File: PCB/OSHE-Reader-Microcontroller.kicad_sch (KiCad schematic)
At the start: 5 parts

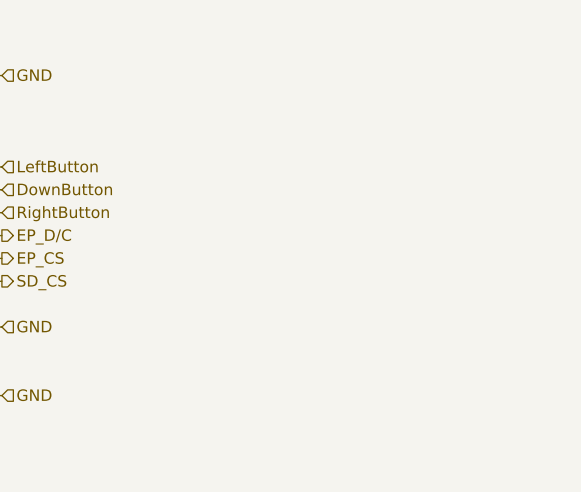
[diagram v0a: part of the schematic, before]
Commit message: Added a bunch of test points to schematic and pcb, hopefully not needed, but good to have :)
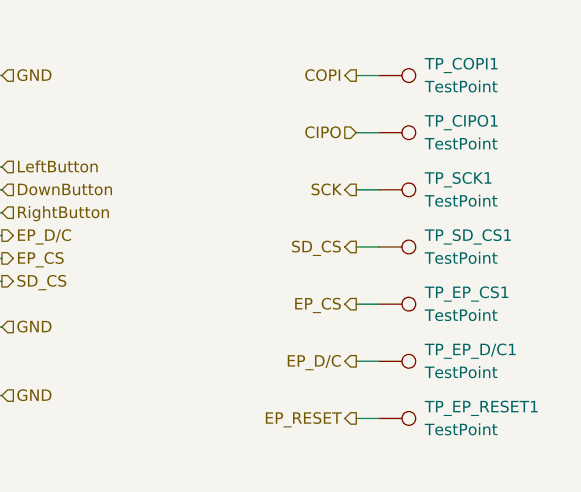
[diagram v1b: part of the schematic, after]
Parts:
- added TP_CIPO1, TP_COPI1, TP_EP_CS1, TP_EP_D/C1, TP_EP_RESET1, TP_SCK1, TP_SD_CS1: TestPoint, TestPoint:TestPoint_Keystone_5019_Miniature, symbol Connector:TestPoint
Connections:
- net CIPO: now also TP_CIPO1.1
- net COPI: now also TP_COPI1.1
- net EP_CS: now also TP_EP_CS1.1
- net EP_D/C: now also TP_EP_D/C1.1
- net EP_RESET: now also TP_EP_RESET1.1
- net SCK: now also TP_SCK1.1
- net SD_CS: now also TP_SD_CS1.1

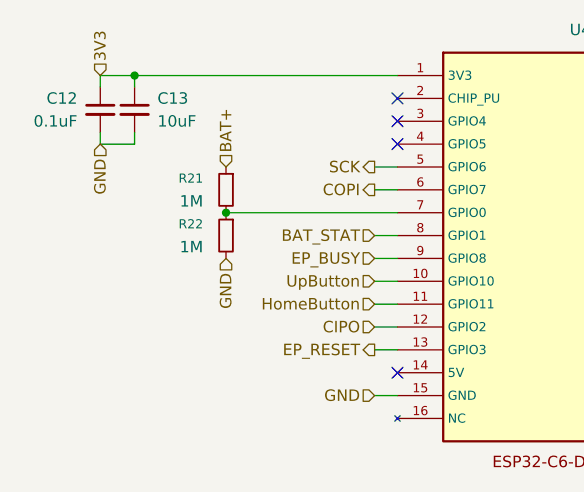
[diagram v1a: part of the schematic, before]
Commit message: Finishing touches with renaming some components and making auto BOM look cleaner
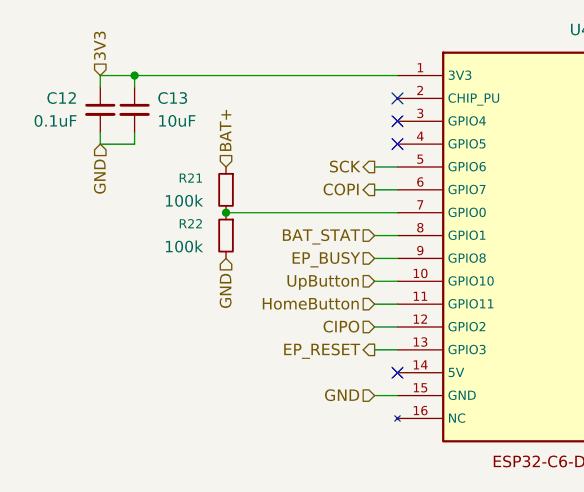
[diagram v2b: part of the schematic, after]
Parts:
- R21, R22: value 1M -> 100k
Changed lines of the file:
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@@
 			)
 		)
-		(property "Value" "1M"
+		(property "Value" "100k"
 			(at 41.91 68.5799 0)
 			(effects
@@
 			)
 		)
-		(property "Value" "1M"
+		(property "Value" "100k"
 			(at 41.91 63.4999 0)
 			(effects

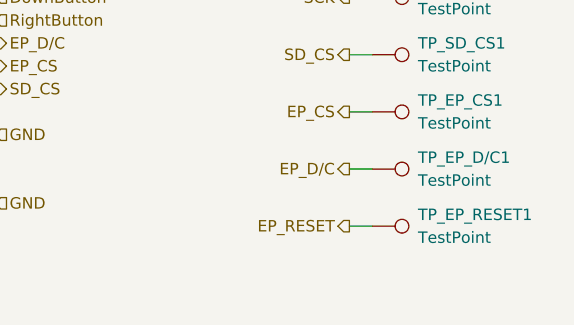
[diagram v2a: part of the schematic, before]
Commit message: Shuffled display connector around for fitting EPD ribbon cable position (also imported dxf for screen + bracket)
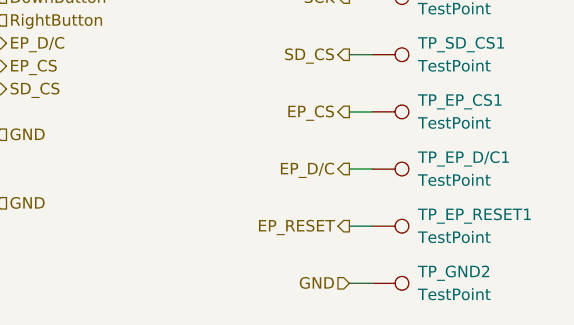
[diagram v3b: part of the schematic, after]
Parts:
- added TP_GND2: TestPoint, TestPoint:TestPoint_Keystone_5019_Miniature, symbol Connector:TestPoint
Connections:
- net GND: now also TP_GND2.1
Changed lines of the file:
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@@
+	(wire
+		(pts
+			(xy 146.05 93.98) (xy 148.59 93.98)
+		)
+		(stroke
+			(width 0)
+			(type default)
+		)
+	)
 	(wire
 		(pts
@@
 		(shape input)
 		(at 60.96 74.93 180)
+		(effects
+			(font
+				(size 1.27 1.27)
+			)
+			(justify right)
+		)
+	)
+	(hierarchical_label "GND"
+		(shape input)
+		(at 146.05 93.98 180)
 		(effects
 			(font
@@
 					(unit 1)
 				)
+			)
+		)
+	)
+	(symbol
+		(lib_id "Connector:TestPoint")
+		(at 148.59 93.98 270)
+		(unit 1)
+		(exclude_from_sim no)
+		(in_bom yes)
+		(on_board yes)
+		(dnp no)
+		(fields_autoplaced yes)
+		(property "Reference" "TP_GND2"
+			(at 153.67 92.7099 90)
+			(effects
+				(font
+					(size 1.27 1.27)
+				)
+				(justify left)
+			)
+		)
+		(property "Value" "TestPoint"
+			(at 153.67 95.2499 90)
+			(effects
+				(font
+					(size 1.27 1.27)
+				)
+				(justify left)
+			)
+		)
+		(property "Footprint" "TestPoint:TestPoint_Keystone_5019_Miniature"
+			(at 148.59 99.06 0)
+			(effects
+				(font
+					(size 1.27 1.27)
+				)
+				(hide yes)
+			)
+		)
+		(property "Datasheet" "~"
+			(at 148.59 99.06 0)
+			(effects
+				(font
+					(size 1.27 1.27)
+				)
+				(hide yes)
+			)
+		)
+		(property "Description" "test point"
+			(at 148.59 93.98 0)
+			(effects
+				(font
+					(size 1.27 1.27)
+				)
+				(hide yes)
+			)
+		)
+		(pin "1"
+		)
+		(instances
+			(project "OSHE-Reader-PCB"
+				(path "/3f072c92-e35a-4654-839b-728bd3dc3a46/03424bf7-051b-4358-a08a-8020da2e6def"
+					(reference "TP_GND2")
+					(unit 1)
+				)

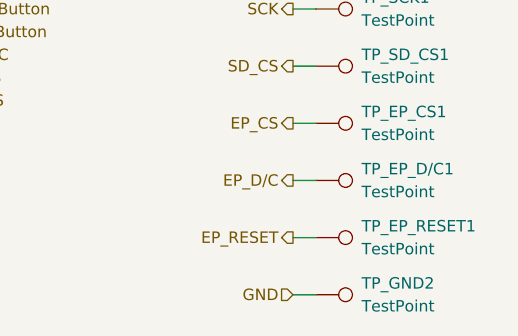
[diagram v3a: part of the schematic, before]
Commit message: Did a bunch of work: - Updated footprint libs with proper 3d models to fix models dissapearing on update from pcb - Updated footprint libs with better silkscreen for drc - Re-did ESP32-C6 Footprint to support through hole AND castellated edges (espressif & waveshare) - Rerouted PCB around new MCU footprint - Minor cleanup on schematic + extra GND test point for convienience using O-Scope
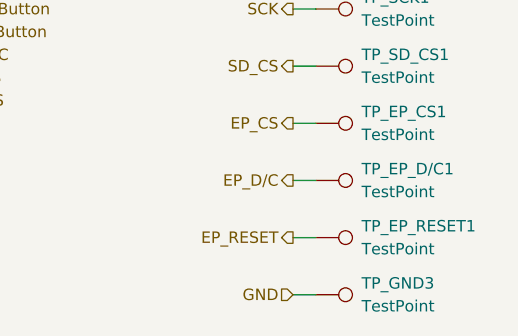
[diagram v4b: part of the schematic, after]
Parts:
- renumbered TP_GND2 to TP_GND3
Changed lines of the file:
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@@
 		(dnp no)
 		(fields_autoplaced yes)
-		(property "Reference" "TP_GND2"
+		(property "Reference" "TP_GND3"
 			(at 153.67 92.7099 90)
 			(effects
@@
 			(project "OSHE-Reader-PCB"
 				(path "/3f072c92-e35a-4654-839b-728bd3dc3a46/03424bf7-051b-4358-a08a-8020da2e6def"
-					(reference "TP_GND2")
+					(reference "TP_GND3")
 					(unit 1)
 				)

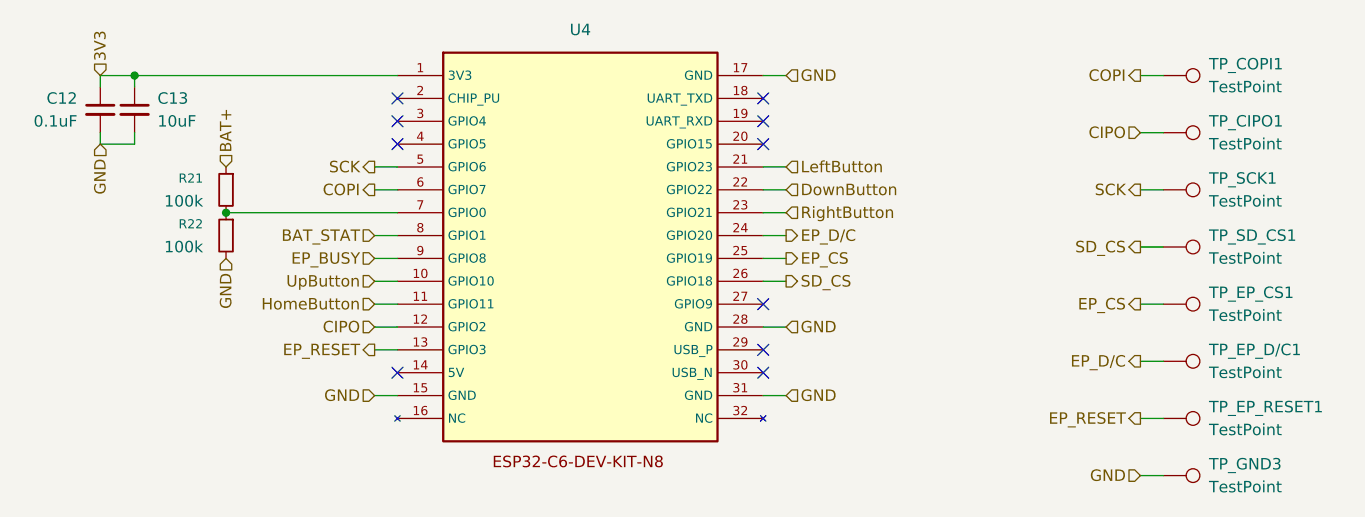
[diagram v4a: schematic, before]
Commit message: Last updates for PCB order. Added revision number, fanicied logo, finished button positions, TODO: Blizzard T. Husky signature :P
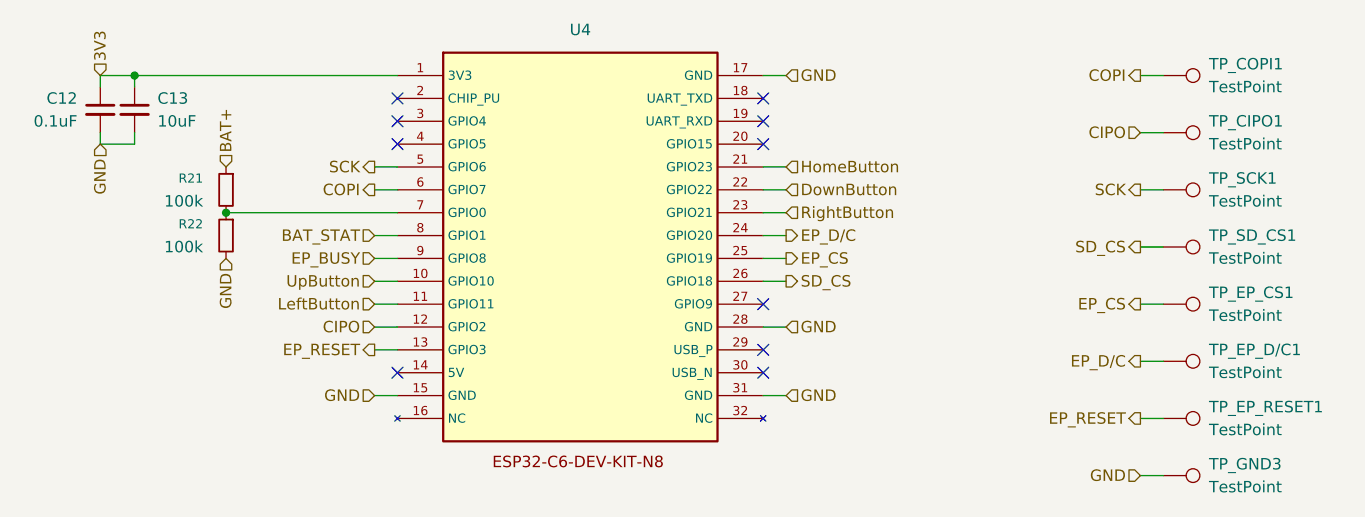
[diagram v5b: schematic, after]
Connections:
- net HomeButton: now also U4.21 (GPIO23); no longer U4.11 (GPIO11)
- net LeftButton: now also U4.11 (GPIO11); no longer U4.21 (GPIO23)
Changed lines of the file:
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@@
 		)
 	)
-	(hierarchical_label "LeftButton"
+	(hierarchical_label "HomeButton"
 		(shape input)
 		(at 106.68 59.69 0)
@@
 		)
 	)
-	(hierarchical_label "HomeButton"
+	(hierarchical_label "LeftButton"
 		(shape input)
 		(at 60.96 74.93 180)

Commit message: Minor fixes to PCB: schottky diode for battery charging and general battery charging routing fixes
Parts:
- U4: value ~ -> (none)
